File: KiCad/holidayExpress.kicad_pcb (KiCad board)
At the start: 2 copper layers, 50 x 50 mm, 22 parts, among them J1 motorPower, J2 motorPower, J3 batteryPower, J4 UARTprogrammer, U1 ESP32-PICO-MINI-02, U2 DRV8833PW, U3 MPM3610GQV-P

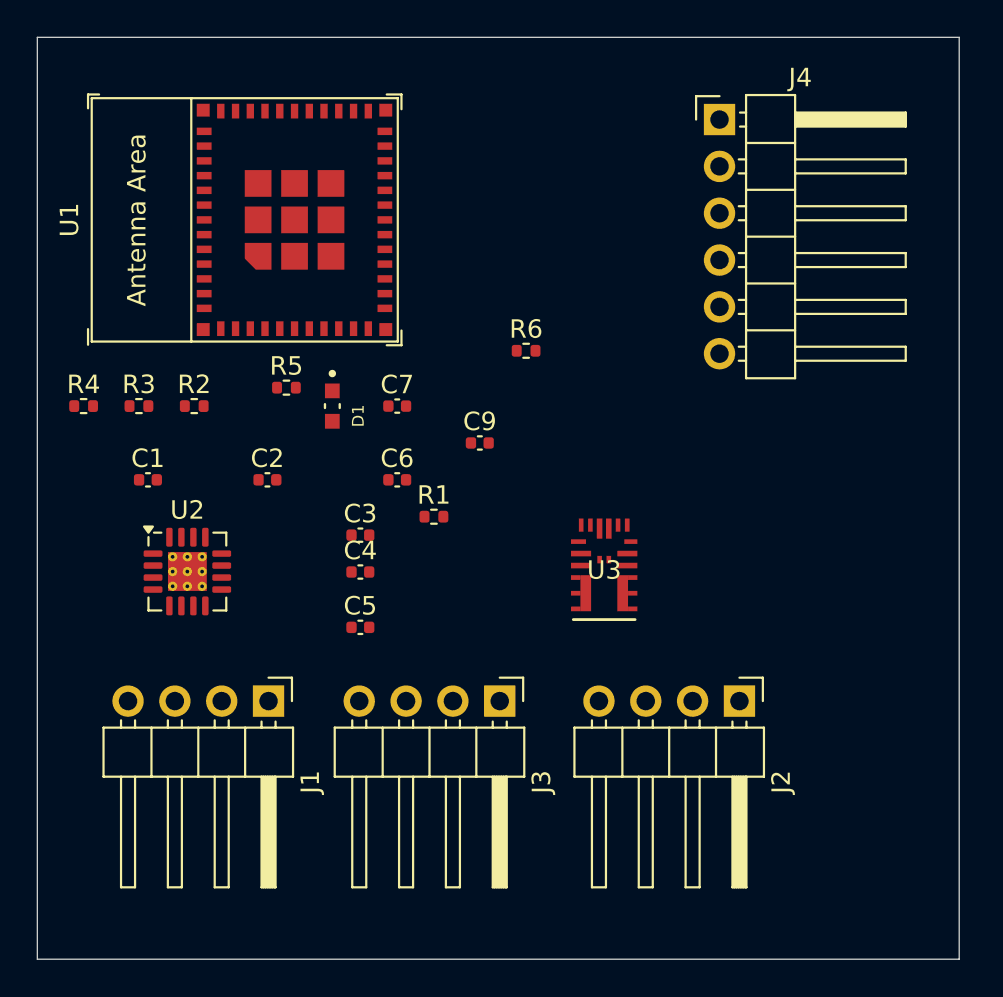
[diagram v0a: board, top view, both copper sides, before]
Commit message: complete initial PCB trace routing
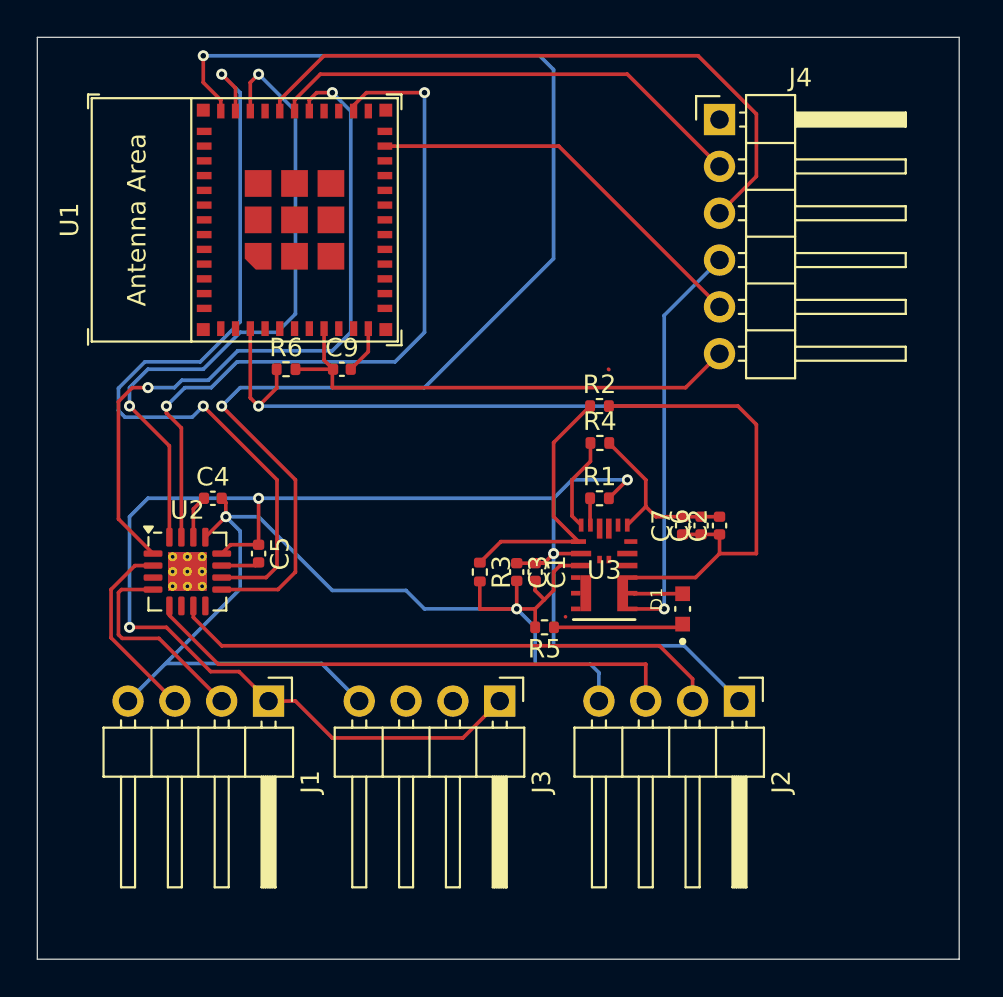
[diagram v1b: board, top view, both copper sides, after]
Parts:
- moved R4 28.1 mm to (188.5, 100.0)
- moved C2 24.6 mm to (195.0, 104.5), turned to 90 degrees
- moved R2 22.0 mm to (188.5, 98.0)
- moved D1 22.0 mm to (193.0, 109.0), turned to 90 degrees
- moved C1 21.6 mm to (185.0, 107.0), turned to -90 degrees
- moved R3 20.6 mm to (182.0, 107.0), turned to -90 degrees
- moved R5 19.1 mm to (185.5, 110.0), turned to 180 degrees
- moved C7 16.8 mm to (193.0, 104.5), turned to 90 degrees
- moved C6 16.7 mm to (194.0, 104.5), turned to 90 degrees
- moved R6 13.1 mm to (171.5, 96.0)
- moved R1 9.04 mm to (188.5, 103.0)
- moved C4 8.94 mm to (167.5, 103.0)
- moved C3 8.71 mm to (184.0, 107.0), turned to -90 degrees
- moved C9 8.48 mm to (174.5, 96.0)
- moved C5 6.82 mm to (170.0, 106.0), turned to -90 degrees
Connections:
- C2 pad 1: +3V3 -> +3.3V
- C9 pad 1: Net-(J4-Pin_5) -> Net-(J4-Pin_6)
- D1 pad A: +3V3 -> +3.3V
- R2 pad 2: +3V3 -> +3.3V
- R6 pad 2: Net-(J4-Pin_5) -> Net-(J4-Pin_6)
- U1 pad 23: Net-(J4-Pin_6) -> Net-(J4-Pin_5)
- U1 pad 8: Net-(J4-Pin_5) -> Net-(J4-Pin_6)
- U2 pad 2: Net-(J1-Pin_2) -> Net-(J1-Pin_3)
- U2 pad 4: Net-(J1-Pin_3) -> Net-(J1-Pin_2)
- U3 pad 7: +3V3 -> +3.3V
- U3 pad 8: +3V3 -> +3.3V
- U3 pad 9: +3V3 -> +3.3V
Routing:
- net VCC: track 0.00 -> 86.9 mm, vias 0 -> 4
- net +3.3V: track 0.00 -> 79.1 mm, vias 0 -> 2
- net GND: track 0.00 -> 78.1 mm, vias 0 -> 2
- net Net-(U1-GPIO21): track 0.00 -> 69.3 mm, vias 0 -> 2
- net Net-(U1-GPIO22): track 0.00 -> 44.1 mm, vias 0 -> 2
- net Net-(U1-GPIO20): track 0.00 -> 40.5 mm, vias 0 -> 2
- net Net-(U1-GPIO5): track 0.00 -> 38.6 mm, vias 0 -> 2
- net Net-(U1-GPIO19): track 0.00 -> 35.7 mm, vias 0 -> 2
- net Net-(J4-Pin_3): track 0.00 -> 35.0 mm
- net Net-(J2-Pin_2): track 0.00 -> 30.3 mm
- net Net-(J2-Pin_3): track 0.00 -> 29.4 mm
- net Net-(J4-Pin_6): track 0.00 -> 27.2 mm
- net Net-(J4-Pin_2): track 0.00 -> 26.3 mm
- net Net-(J4-Pin_5): track 0.00 -> 21.8 mm
- net Net-(U3-FB): track 0.00 -> 14.6 mm
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
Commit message: add ground plane and optimize routing
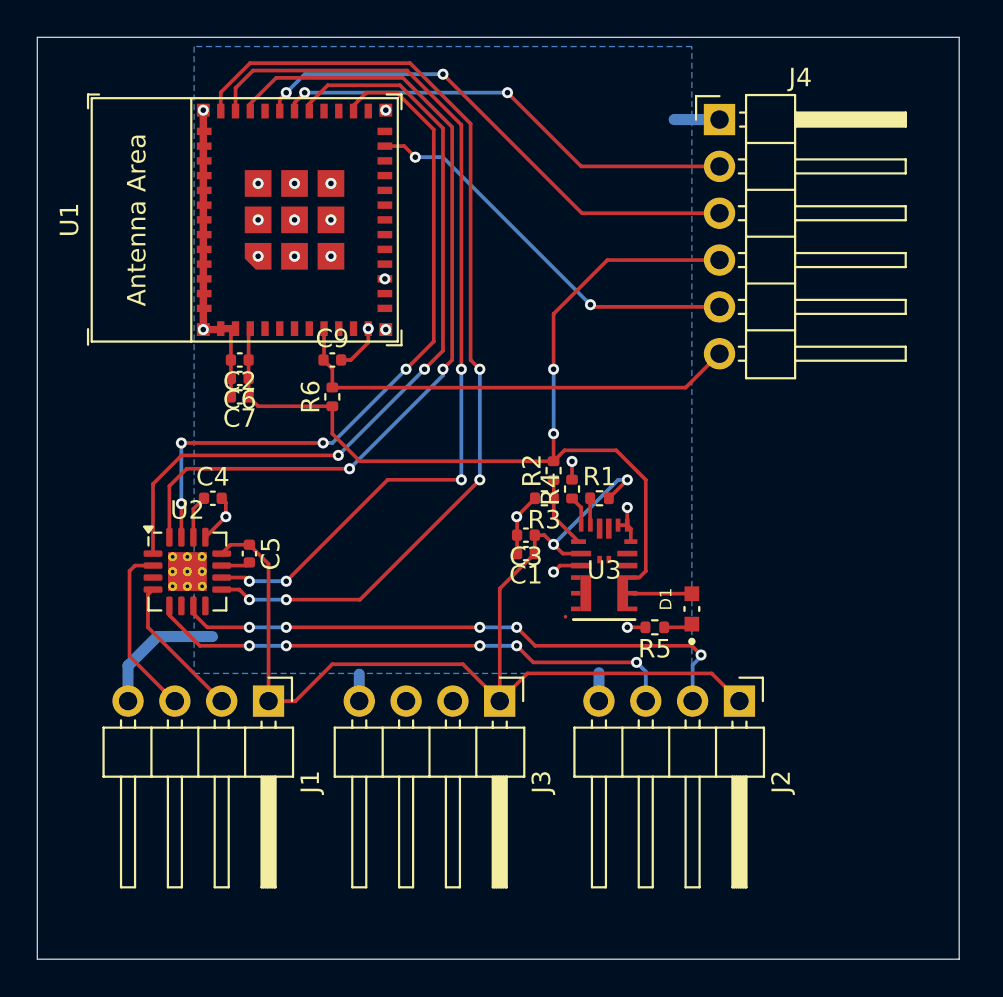
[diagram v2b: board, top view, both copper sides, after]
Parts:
- moved C2 27.5 mm to (169.0, 95.5), turned to 180 degrees
- moved C6 26.3 mm to (169.0, 96.5), turned to 180 degrees
- moved C7 25.0 mm to (169.0, 97.5), turned to 180 degrees
- moved R5 5.98 mm to (191.5, 110.0)
- moved R3 5.32 mm to (185.5, 103.0), turned to 180 degrees
- moved R2 4.30 mm to (186.0, 101.5), turned to 90 degrees
- moved R6 2.92 mm to (174.0, 97.5), turned to 90 degrees
- moved R4 2.92 mm to (187.0, 102.5), turned to 90 degrees
- moved C3 2.06 mm to (184.5, 105.0), turned to 180 degrees
- moved C1 1.12 mm to (184.5, 106.0), turned to 180 degrees
- moved C9 0.72 mm to (174.0, 95.5)
- moved C5 0.50 mm to (169.5, 106.0)
- moved D1 0.50 mm to (193.5, 109.0)
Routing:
- net GND: track 78.1 -> 46.0 mm, vias 2 -> 21
- net VCC: track 86.9 -> 58.6 mm, vias 4 -> 2
- net +3.3V: track 79.1 -> 55.8 mm
- net Net-(U1-GPIO21): track 69.3 -> 53.0 mm, vias 2 -> 4
- net Net-(U1-GPIO19): track 35.7 -> 46.8 mm
- net Net-(U3-FB): track 14.6 -> 3.90 mm
- net Net-(J4-Pin_3): track 35.0 -> 28.2 mm, vias 0 -> 2
- net Net-(U1-GPIO22): track 44.1 -> 49.7 mm, vias 2 -> 4
- net Net-(D1-PadC): track 7.05 -> 1.57 mm
- net Net-(U1-GPIO5): track 38.6 -> 43.6 mm
- net Net-(J1-Pin_2): track 11.3 -> 7.82 mm
- net Net-(U3-AAM): track 5.08 -> 1.65 mm
- net Net-(U1-GPIO20): track 40.5 -> 38.3 mm, vias 2 -> 4
- net Net-(J4-Pin_6): track 27.2 -> 25.1 mm
- net Net-(J2-Pin_2): track 30.3 -> 31.6 mm, vias 0 -> 5
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- added copper zone on B.Cu, net GND

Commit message: adjust clearances and start DRC fixes
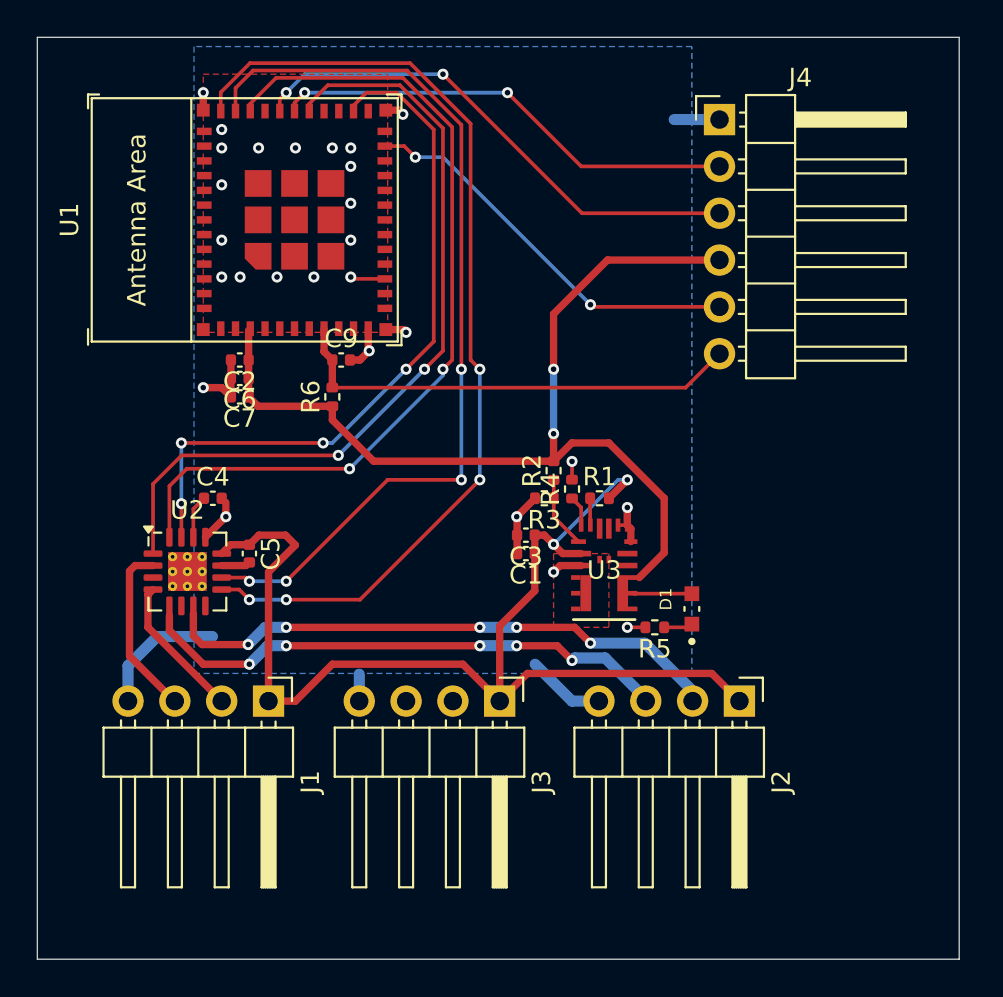
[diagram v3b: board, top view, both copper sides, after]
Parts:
- moved C9 0.48 mm to (174.5, 95.5)
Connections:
- U3 pad 4: unconnected-(U3-SW-Pad4) -> Net-(U3-SW-Pads-4-5-6)
- U3 pad 5: unconnected-(U3-SW-Pad5) -> Net-(U3-SW-Pads-4-5-6)
- U3 pad 6: unconnected-(U3-SW-Pad6) -> Net-(U3-SW-Pads-4-5-6)
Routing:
- net GND: track 46.0 -> 40.4 mm, vias 21 -> 27
- net VCC: track 58.6 -> 61.7 mm
- net +3.3V: track 55.8 -> 56.5 mm
- net Net-(J2-Pin_3): track 29.2 -> 29.8 mm
- added copper zone on F.Cu, net GND
- added copper zone on F.Cu, net Net-(U3-SW-Pads-4-5-6)

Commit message: add silkscreen labels and clear DRC errors
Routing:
- added copper zone on F.Cu, net +3.3V
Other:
- board text added: "3v3"
- board text added: "BOOT"
- board text added: "EN"
- board text added: "GND"
- board text added: "RXD"
- board text added: "TXD"
- board text added: "holidayExpress 0.0 Bad Hippo Design"

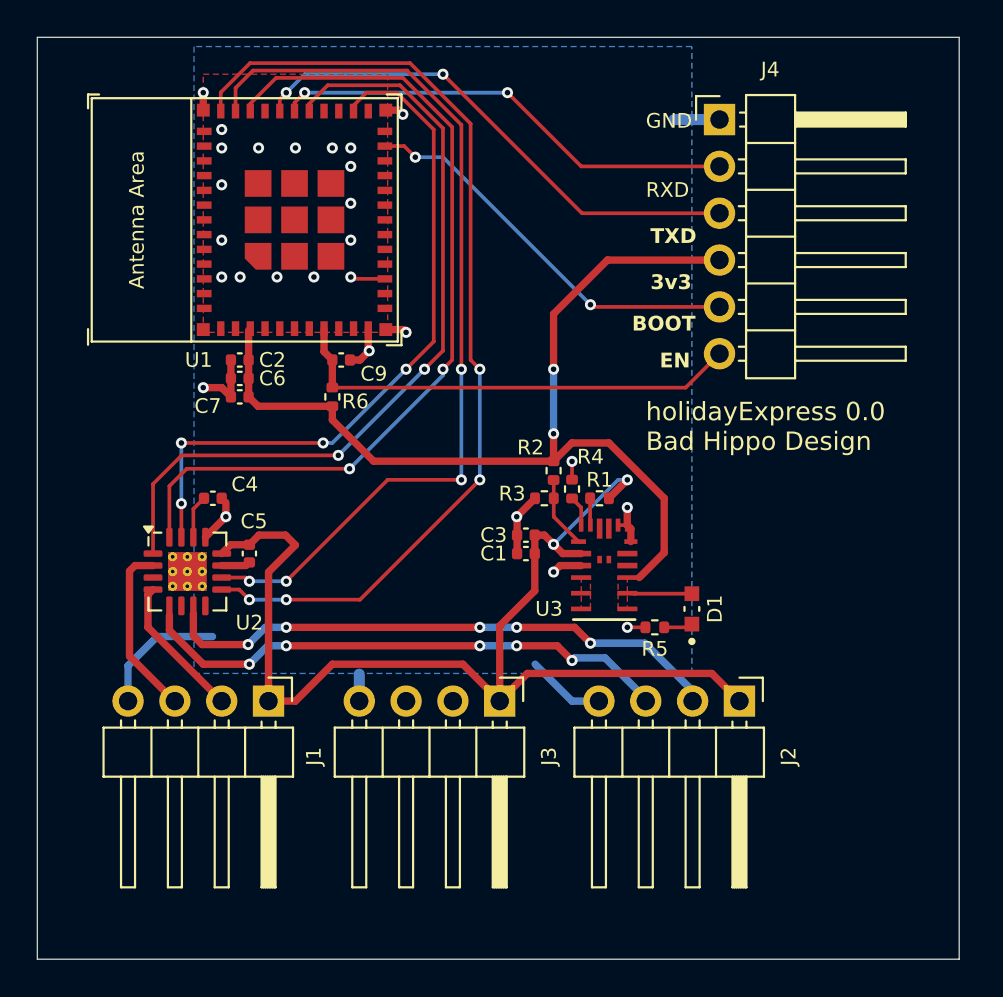
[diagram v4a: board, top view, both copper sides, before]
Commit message: add LCSC part numbers to symbols
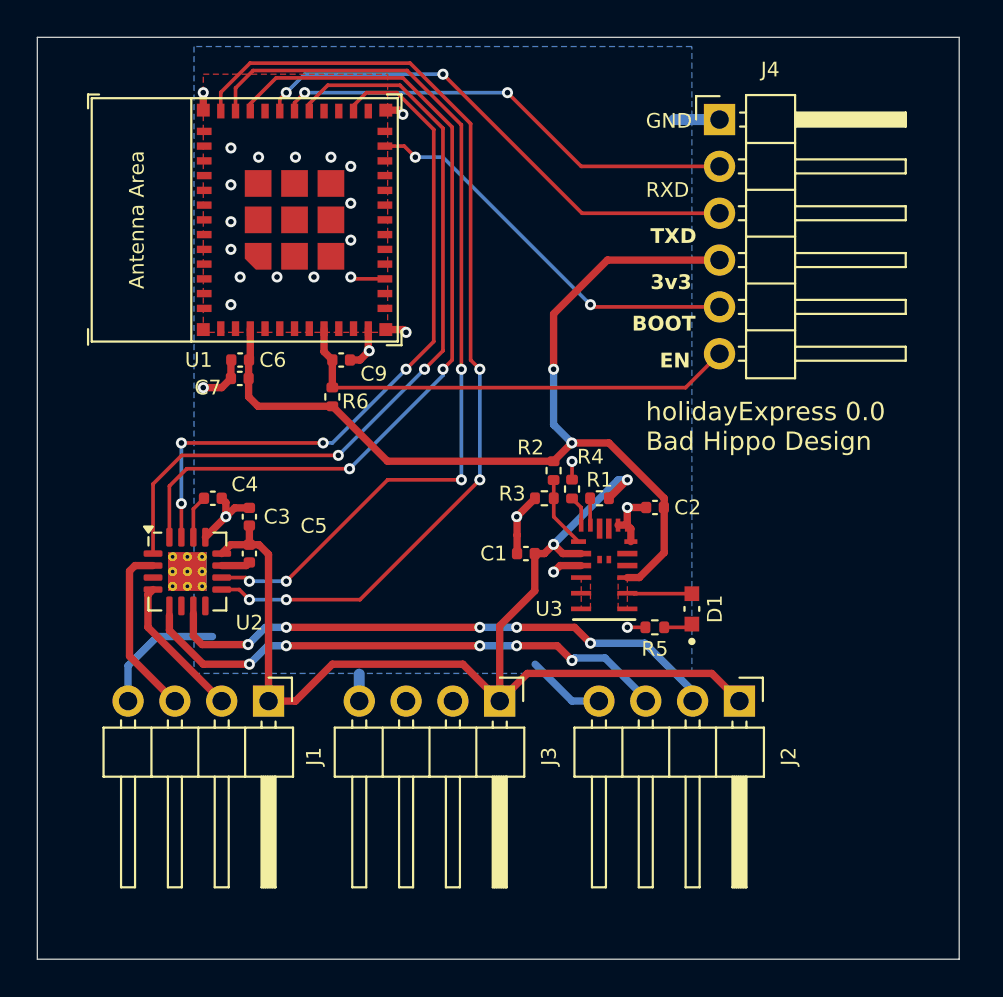
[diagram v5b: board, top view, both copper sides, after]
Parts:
- C1, C3, C9: value 10 -> 10uF
- C2, C6: value 22 -> 22uF
- C4: value 2.2 -> 2.2uF
- C5: value 0.01 -> 0.01uF
- C7: value 0.1 -> 0.1uF
- moved C2 23.9 mm to (191.5, 103.5)
- moved C3 15.0 mm to (169.5, 104.0), turned to 90 degrees
- moved C6 1.00 mm to (169.0, 95.5)
- moved C7 1.00 mm to (169.0, 96.5)
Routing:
- net VCC: track 61.7 -> 59.0 mm
- net GND: track 40.4 -> 41.6 mm, vias 27 -> 26
- net +3.3V: track 56.5 -> 55.9 mm

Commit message: correct MPM3610 power input errors
Connect MPM3610 In pin to power, make VCC unconnected. Re-orient UART programmer pins so that direct connection can be used with esp flashy tool. Reorient and optimize PCB layout around MPM changes, add copper pours and larger power traces.
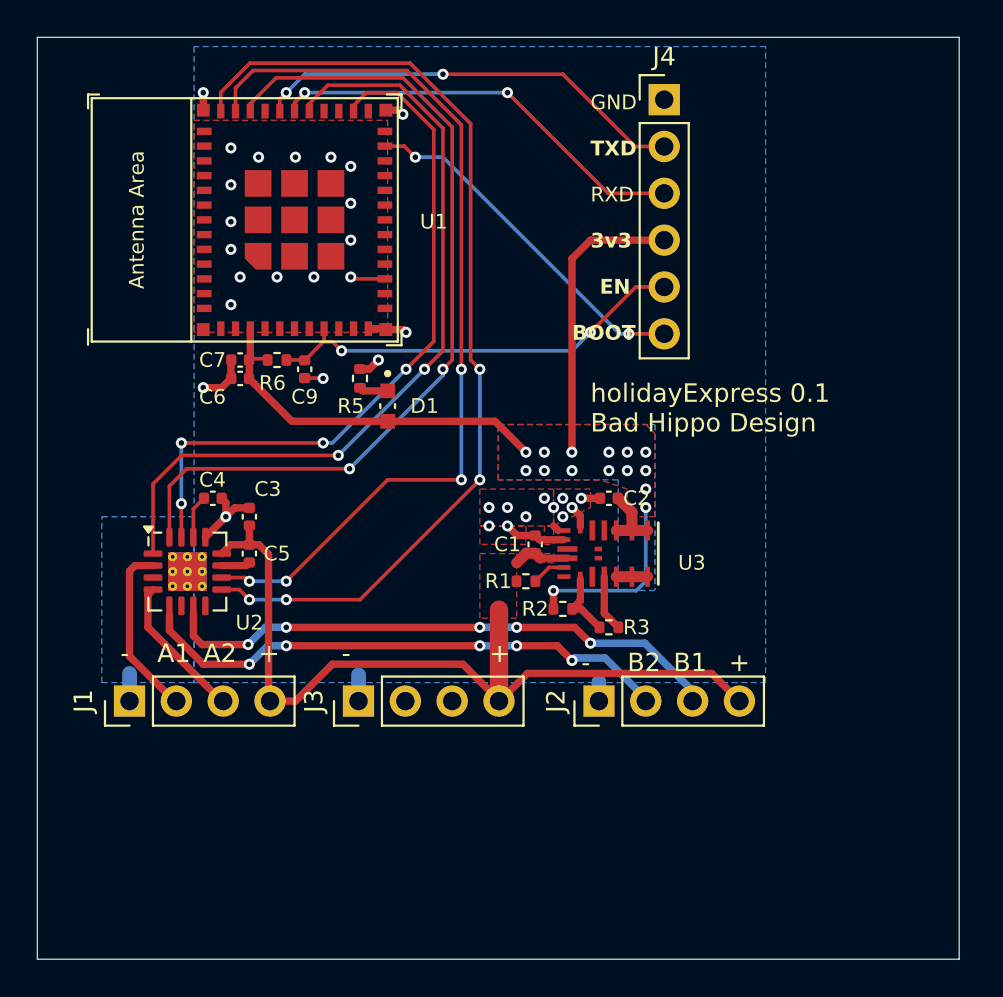
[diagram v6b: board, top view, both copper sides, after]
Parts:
- removed R4: 54k, Resistor_SMD:R_0402_1005Metric
- J1, J2, J3: footprint Connector_PinHeader_2.54mm:PinHeader_1x04_P2.54mm_Horizontal -> Connector_PinHeader_2.54mm:PinHeader_1x04_P2.54mm_Vertical
- J4: footprint Connector_PinHeader_2.54mm:PinHeader_1x06_P2.54mm_Horizontal -> Connector_PinHeader_2.54mm:PinHeader_1x06_P2.54mm_Vertical
- U2: value DRV8833PW -> DRV8833
- moved R5 20.9 mm to (175.5, 96.5), turned to 90 degrees
- moved D1 19.8 mm to (177.0, 98.0), turned to -90 degrees
- moved R3 7.83 mm to (189.0, 110.0), turned to 0 degrees
- moved J3 7.66 mm to (175.4, 114.0), turned to 90 degrees
- moved J2 7.62 mm to (188.5, 114.0), turned to 90 degrees
- moved J1 7.54 mm to (163.0, 114.0), turned to 90 degrees
- moved R2 7.52 mm to (186.5, 109.0), turned to 180 degrees
- moved R1 6.01 mm to (184.5, 107.5), turned to 180 degrees
- moved R6 3.61 mm to (171.0, 95.5), turned to 0 degrees
- moved J4 3.19 mm to (192.0, 81.4)
- moved C2 2.55 mm to (189.0, 103.0)
- moved C9 2.04 mm to (172.5, 96.0), turned to -90 degrees
- moved C7 1.00 mm to (169.0, 95.5)
- moved C6 1.00 mm to (169.0, 96.5)
- moved U3 0.94 mm to (189.0, 106.0), turned to 90 degrees
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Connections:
- C1 pad 1: VCC -> +9V
- C3 pad 1: VCC -> +9V
- C5 pad 1: VCC -> +9V
- C9 pad 1: Net-(J4-Pin_6) -> Net-(J4-Pin_5)
- J1 pad 1: VCC -> GND
- J1 pad 4: GND -> +9V
- J2 pad 1: VCC -> GND
- J2 pad 4: GND -> +9V
- J3 pad 1: VCC -> GND
- J3 pad 4: GND -> +9V
- R1 pad 2: VCC -> +9V
- R3 pad 2: GND -> Net-(U3-AGND)
- R6 pad 2: Net-(J4-Pin_6) -> Net-(J4-Pin_5)
- U1 pad 23: Net-(J4-Pin_5) -> Net-(J4-Pin_6)
- U1 pad 30: Net-(J4-Pin_2) -> Net-(J4-Pin_3)
- U1 pad 31: Net-(J4-Pin_3) -> Net-(J4-Pin_2)
- U1 pad 8: Net-(J4-Pin_6) -> Net-(J4-Pin_5)
- U2 pad 12: VCC -> +9V
- U2 pad 2: Net-(J1-Pin_3) -> Net-(J1-Pin_2)
- U2 pad 4: Net-(J1-Pin_2) -> Net-(J1-Pin_3)
- U2 pad 5: Net-(J2-Pin_3) -> Net-(J2-Pin_2)
- U2 pad 7: Net-(J2-Pin_2) -> Net-(J2-Pin_3)
- U3 pad 16: unconnected-(U3-IN-Pad16) -> +9V
- U3 pad 18: Net-(U3-AAM) -> unconnected-(U3-AAM-Pad18)
- U3 pad 2: VCC -> unconnected-(U3-VCC-Pad2)
- U3 pad 3: GND -> Net-(U3-AGND)
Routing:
- net VCC: track 59.0 -> 0.00 mm, vias 2 -> 0
- net +9V: track 0.00 -> 48.4 mm
- net GND: track 41.6 -> 26.5 mm, vias 26 -> 33
- net Net-(J4-Pin_6): track 25.1 -> 19.4 mm, vias 0 -> 2
- net +3.3V: track 55.9 -> 50.5 mm, vias 2 -> 15
- net Net-(J4-Pin_3): track 28.2 -> 23.0 mm
- net Net-(U3-AGND): track 0.00 -> 3.06 mm
- net Net-(J4-Pin_2): track 25.4 -> 23.7 mm
- net Net-(U3-SW-Pad4): track 0.00 -> 1.70 mm
- net Net-(J1-Pin_3): track 9.49 -> 7.82 mm
- net Net-(J1-Pin_2): track 7.82 -> 9.49 mm
- net Net-(U3-AAM): track 1.65 -> 0.00 mm
- net Net-(J4-Pin_5): track 21.8 -> 23.3 mm
- net Net-(J2-Pin_3): track 29.8 -> 31.3 mm
- net Net-(J2-Pin_2): track 31.3 -> 29.8 mm
- added copper zone on B.Cu, net +3.3V
- added copper zone on F.Cu, net +9V
- removed copper zone on F.Cu, net Net-(U3-SW-Pad4)
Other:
- board text added: "+"
- board text added: "-"
- board text added: "A1"
- board text added: "A2"
- board text added: "B1"
- board text added: "B2"
- board text added: "holidayExpress 0.1 Bad Hippo Design"
- board text removed: "holidayExpress 0.0 Bad Hippo Design"
